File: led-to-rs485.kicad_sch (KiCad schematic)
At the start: 9 parts, among them J2 Terminal, U4 MAX485E

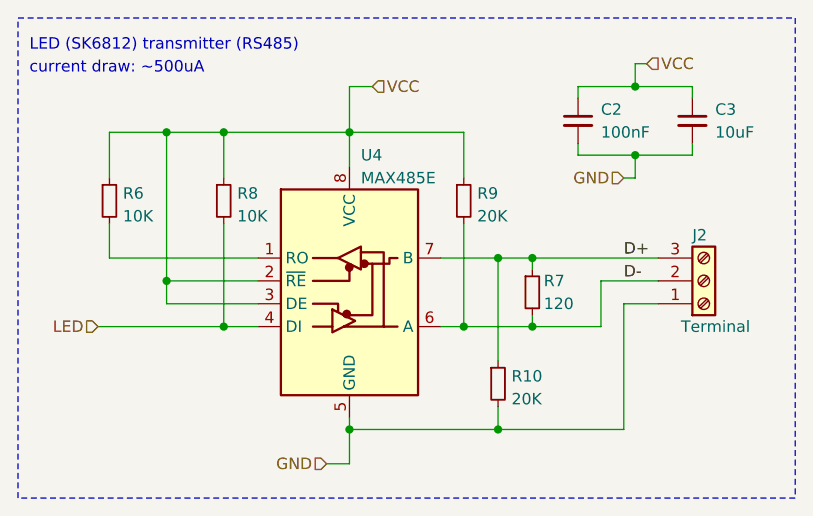
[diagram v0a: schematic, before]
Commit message: Geographically reannotate
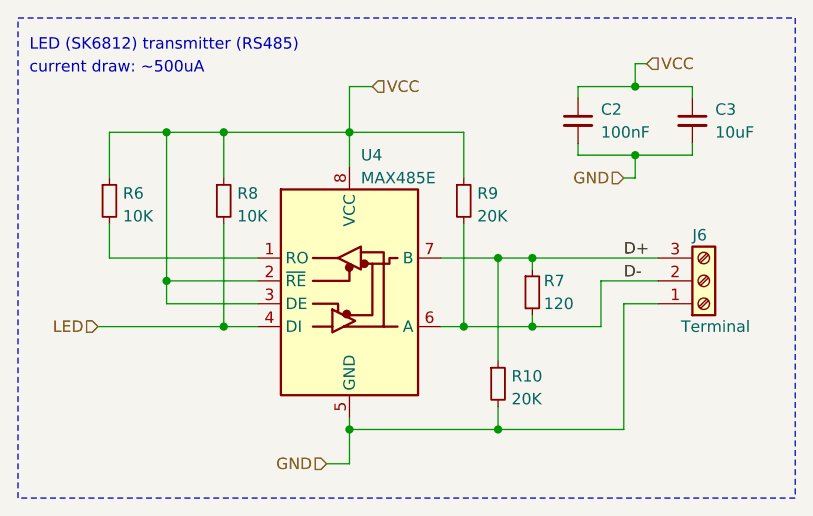
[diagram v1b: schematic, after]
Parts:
- renumbered J2 to J6

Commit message: fix power sources, update reveivers accordingly (main board PCB not updated yet)
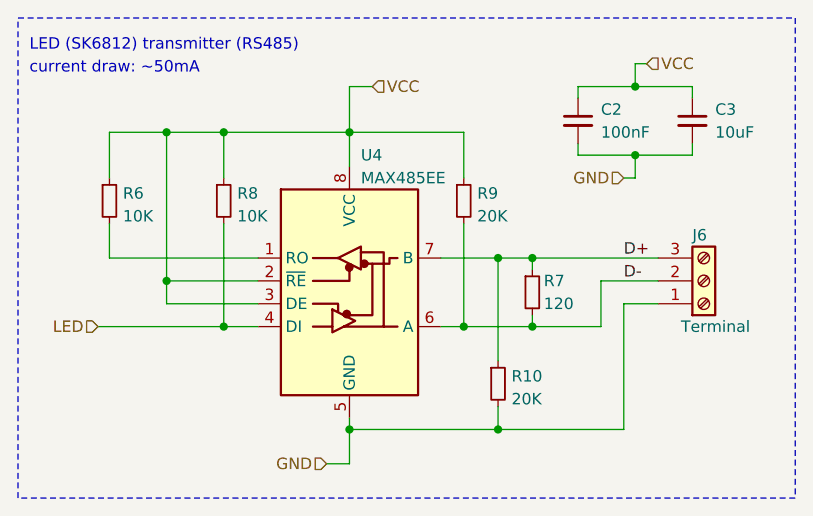
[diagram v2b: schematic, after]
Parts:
- C2, C3: LCSC Part # C1525 -> (none); LCSC Part Number C1525 -> (none)
- R10, R7, R9: LCSC Part # C4328 -> (none); LCSC Part Number C4328 -> (none)
- R6, R8: LCSC Part # C15401 -> (none); LCSC Part Number C15401 -> (none)
- U4: value MAX485E -> MAX485EE
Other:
- note added: "current draw: ~50mA"
- note removed: "current draw: ~500uA"
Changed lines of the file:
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@@
     (effects (font (size 1.27 1.27)) (justify left bottom))
   )
-  (text "current draw: ~500uA" (at 111.76 78.74 0)
+  (text "current draw: ~50mA" (at 111.76 78.74 0)
     (effects (font (size 1.27 1.27) (color 132 132 132 1)) (justify left bottom))
   )
@@
       (effects (font (size 1.27 1.27)) hide)
     )
-    (property "LCSC Part Number" "C1525" (at 172.72 83.82 0)
-      (effects (font (size 1.27 1.27)) hide)
-    )
-    (property "LCSC Part #" "C1525" (at 172.72 83.82 0)
+    (property "LCSC Part Number" "" (at 172.72 83.82 0)
+      (effects (font (size 1.27 1.27)) hide)
+    )
+    (property "LCSC Part #" "" (at 172.72 83.82 0)
       (effects (font (size 1.27 1.27)) hide)
     )
@@
       (effects (font (size 1.27 1.27)) hide)
     )
-    (property "LCSC Part Number" "C15401" (at 120.65 92.71 0)
-      (effects (font (size 1.27 1.27)) hide)
-    )
-    (property "LCSC Part #" "C15401" (at 120.65 92.71 0)
+    (property "LCSC Part Number" "" (at 120.65 92.71 0)
+      (effects (font (size 1.27 1.27)) hide)
+    )
+    (property "LCSC Part #" "" (at 120.65 92.71 0)
       (effects (font (size 1.27 1.27)) hide)
     )
@@
       (effects (font (size 1.27 1.27)) hide)
     )
-    (property "LCSC Part Number" "C1525" (at 185.42 83.82 0)
-      (effects (font (size 1.27 1.27)) hide)
-    )
-    (property "LCSC Part #" "C1525" (at 185.42 83.82 0)
+    (property "LCSC Part Number" "" (at 185.42 83.82 0)
+      (effects (font (size 1.27 1.27)) hide)
+    )
+    (property "LCSC Part #" "" (at 185.42 83.82 0)
       (effects (font (size 1.27 1.27)) hide)
     )
@@
       (effects (font (size 1.27 1.27)) hide)
     )
-    (property "LCSC Part Number" "C4328" (at 163.83 113.03 0)
-      (effects (font (size 1.27 1.27)) hide)
-    )
-    (property "LCSC Part #" "C4328" (at 163.83 113.03 0)
+    (property "LCSC Part Number" "" (at 163.83 113.03 0)
+      (effects (font (size 1.27 1.27)) hide)
+    )
+    (property "LCSC Part #" "" (at 163.83 113.03 0)
       (effects (font (size 1.27 1.27)) hide)
     )
@@
       (effects (font (size 1.27 1.27)) hide)
     )
-    (property "LCSC Part Number" "C15401" (at 133.35 92.71 0)
-      (effects (font (size 1.27 1.27)) hide)
-    )
-    (property "LCSC Part #" "C15401" (at 133.35 92.71 0)
+    (property "LCSC Part Number" "" (at 133.35 92.71 0)
+      (effects (font (size 1.27 1.27)) hide)
+    )
+    (property "LCSC Part #" "" (at 133.35 92.71 0)
       (effects (font (size 1.27 1.27)) hide)
     )
@@
       (effects (font (size 1.27 1.27)) hide)
     )
-    (property "LCSC Part Number" "C4328" (at 167.64 102.87 0)
-      (effects (font (size 1.27 1.27)) hide)
-    )
-    (property "LCSC Part #" "C4328" (at 167.64 102.87 0)
+    (property "LCSC Part Number" "" (at 167.64 102.87 0)
+      (effects (font (size 1.27 1.27)) hide)
+    )
+    (property "LCSC Part #" "" (at 167.64 102.87 0)
       (effects (font (size 1.27 1.27)) hide)
     )
@@
       (effects (font (size 1.27 1.27)) (justify left))
     )
-    (property "Value" "MAX485E" (at 148.59 90.17 0)
+    (property "Value" "MAX485EE" (at 148.59 90.17 0)
       (effects (font (size 1.27 1.27)) (justify left))
     )
@@
       (effects (font (size 1.27 1.27)) hide)
     )
-    (property "LCSC Part Number" "C4328" (at 160.02 92.71 0)
-      (effects (font (size 1.27 1.27)) hide)
-    )
-    (property "LCSC Part #" "C4328" (at 160.02 92.71 0)
-      (effects (font (size 1.27 1.27)) hide)
-    )
+    (property "LCSC Part Number" "" (at 160.02 92.71 0)
+      (effects (font (size 1.27 1.27)) hide)
+    )
+    (property "LCSC Part #" "" (at 160.02 92.71 0)
+      (effects (font (size 1.27 1.27)) hide)
+    )
